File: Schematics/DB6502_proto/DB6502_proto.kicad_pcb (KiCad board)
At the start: 2 copper layers, 132.1 x 104.1 mm, 51 parts, among them J1 System Bus, J10 AVR-ISP-6, J2 Controls, J3 Debug UART, J4 I/O Bus, J5 USB_B, SW1 Reset, U1 DS1813, U2 65C02S, U3 62256, U4 ATmega644PA-PU, U5 62256, U6 74AC138, U7 28C256, U8 22V10C, U9 FT230XS, Y1 20MHz

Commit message: PCB layout RC1
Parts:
- added REF**: OSHW-Logo_5.7x6mm_SilkScreen, Symbol:OSHW-Logo_5.7x6mm_SilkScreen, F.Cu at (71.1, 24.1)
- added REF**: KiCad-Logo2_5mm_SilkScreen, Symbol:KiCad-Logo2_5mm_SilkScreen, F.Cu at (48.9, 49.5)
- moved C3 49.4 mm to (76.2, 104.1), turned to 0 degrees
- moved C9 48.4 mm to (119.4, 80.0), turned to 90 degrees
- moved C1 3.73 mm to (106.6, 104.1), turned to 180 degrees
- moved C10 2.50 mm to (81.3, 45.7), turned to 270 degrees
- moved C5 2.50 mm to (119.4, 54.6), turned to 270 degrees
- moved C8 2.50 mm to (119.4, 31.8), turned to 270 degrees
- moved C2 1.31 mm to (83.8, 104.1)
- moved REF** 0.63 mm to (43.2, 17.8)
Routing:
- net +5V: track 0.00 -> 473.8 mm, vias 0 -> 12
- net d1: track 0.00 -> 288.2 mm, vias 0 -> 6
- net d0: track 0.00 -> 279.0 mm, vias 0 -> 6
- net ~6502_RES: track 0.00 -> 265.6 mm, vias 0 -> 8
- net d5: track 0.00 -> 261.4 mm, vias 0 -> 1
- net d2: track 0.00 -> 261.3 mm, vias 0 -> 4
- net d3: track 0.00 -> 252.5 mm, vias 0 -> 2
- net d6: track 0.00 -> 248.9 mm, vias 0 -> 2
- net d4: track 0.00 -> 246.8 mm, vias 0 -> 2
- net GND: track 0.00 -> 240.7 mm, vias 0 -> 5
- net d7: track 0.00 -> 239.2 mm, vias 0 -> 3
- net R~W: track 0.00 -> 237.7 mm, vias 0 -> 9
- net a0: track 0.00 -> 230.9 mm, vias 0 -> 6
- net a1: track 0.00 -> 228.6 mm, vias 0 -> 6
- net a2: track 0.00 -> 221.5 mm, vias 0 -> 6
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- added copper zone on B.Cu, net GND
- added copper zone on F.Cu, net GND
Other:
- board size 132.1 x 104.1 mm -> 133.3 x 105.4 mm
- net class Default: clearance 0.2 -> 0.1; trace_width 0.25 -> 0.2; via_dia 0.8 -> 0.6
- net class POWER added: clearance 0.1, trace_width 0.25, via_dia 0.6, via_drill 0.4
- rule trace_clearance: 0.2 -> 0.1
- board text added: "+5V"
- board text added: "20MHz"
- board text added: "32KB RAM1"
- board text added: "32KB RAM2"
- board text added: "32KB ROM"
- board text added: "6502 CPU"
- board text added: "6502 Prototype Board Designed by Dawid Buchwald https://github.com/dbuchwald/6502"
- board text added: "A00"
- board text added: "A01"
- board text added: "A02"
- board text added: "A03"
- board text added: "A04"
- board text added: "A05"
- board text added: "A06"
- board text added: "A07"
- board text added: "A08"
- board text added: "A09"
- board text added: "A10"
- board text added: "A11"
- board text added: "A12"
- board text added: "A13"
- board text added: "A14"
- board text added: "A15"
- board text added: "ATmega644PA Supervisor"
- board text added: "AVR ISP"
- board text added: "BE"
- board text added: "CLD"
- board text added: "CLK"
- board text added: "Control Bus"
- board text added: "Control pull-up resistors"
- board text added: "D0"
- board text added: "D1"
- board text added: "D2"
- board text added: "D3"
- board text added: "D4"
- board text added: "D5"
- board text added: "D6"
- board text added: "D7"
- board text added: "EXR"
- board text added: "GND"
- board text added: "I/O Selector"
- board text added: "I12"
- board text added: "IO"
- board text added: "Input/Output Bus"
- board text added: "O13"
- board text added: "O14"
- board text added: "O15"
- board text added: "O16"
- board text added: "Programmable Logic Array"
- board text added: "RDY"
- board text added: "RESET"
- board text added: "RxD"
- board text added: "R~W"
- board text added: "SNC"
- board text added: "SRC"
- board text added: "SRD"
- board text added: "SRO"
- board text added: "System Bus"
- board text added: "TxD"
- board text added: "UART"
- board text added: "USB"
- board text added: "~6RS"
- board text added: "~CTS"
- board text added: "~IO0"
- board text added: "~IO1"
- board text added: "~IO2"
- board text added: "~IO3"
- board text added: "~IRQ"
- board text added: "~LAT"
- board text added: "~ML"
- board text added: "~NMI"
- board text added: "~OE"
- board text added: "~RES"
- board text added: "~RM1"
- board text added: "~RM2"
- board text added: "~ROM"
- board text added: "~RST"
- board text added: "~RTS"
- board text added: "~SO"
- board text added: "~URT"
- board text added: "~VI1"
- board text added: "~VI2"
- board text added: "~VP"
- board text added: "~WE"

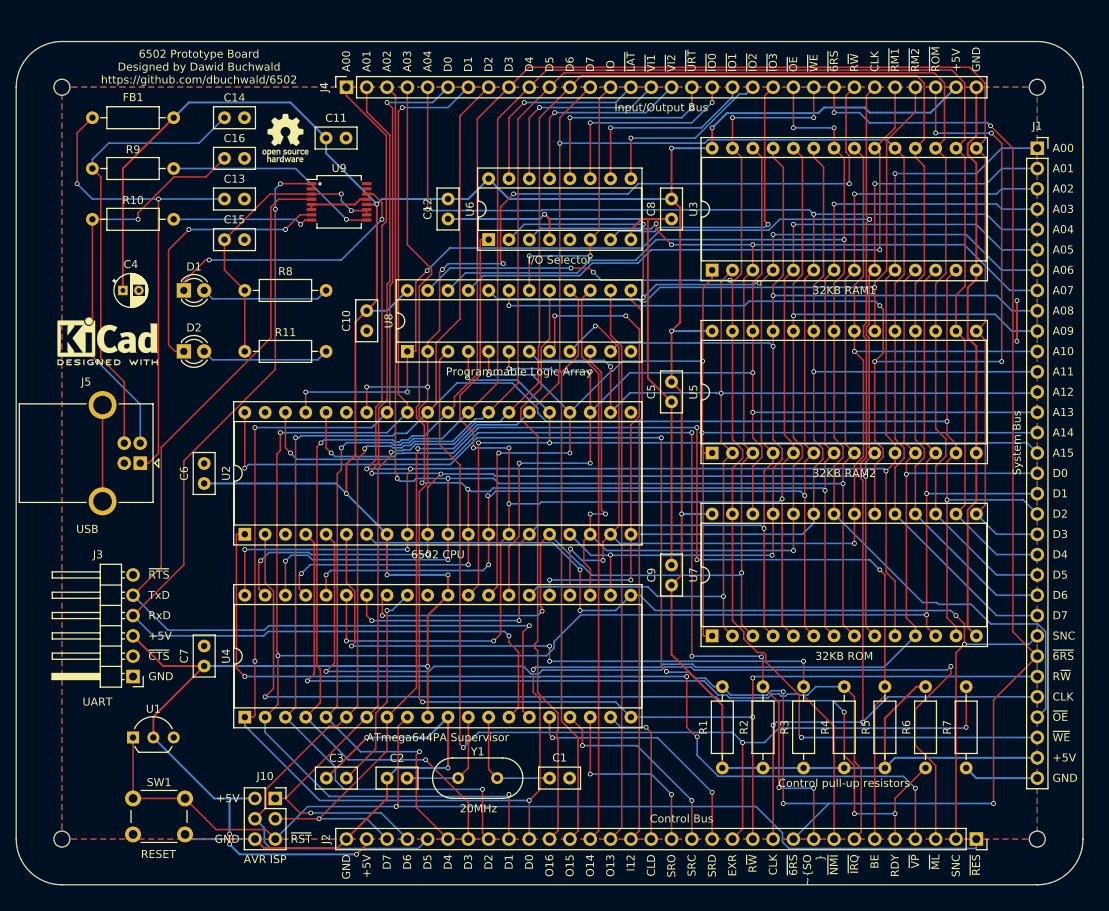
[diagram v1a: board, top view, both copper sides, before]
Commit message: Ordered DB6502 proto PCB
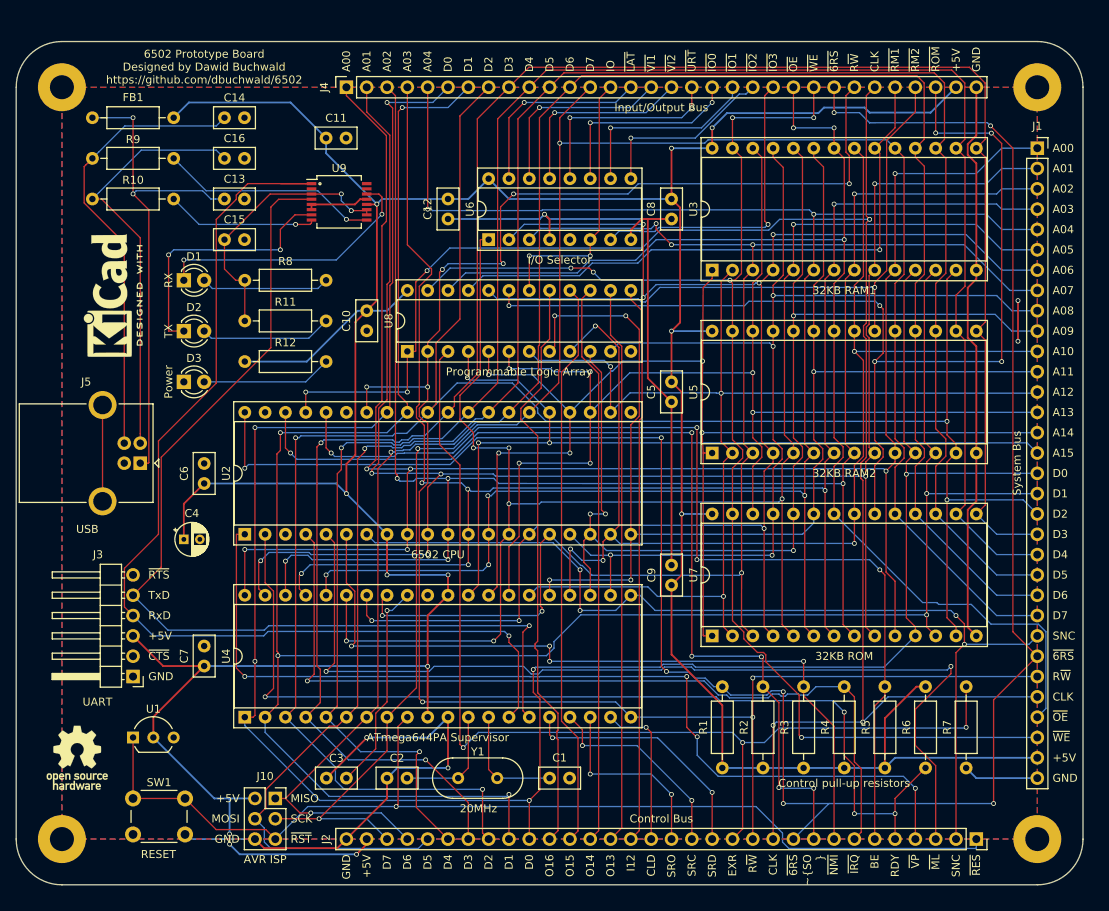
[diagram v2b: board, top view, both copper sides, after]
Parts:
- removed the REF** at (71.1, 24.1)
- removed the REF** at (48.9, 49.5)
- removed the REF** at (43.2, 17.8)
- removed the REF** at (43.2, 111.8)
- removed the REF** at (165.1, 111.8)
- removed the REF** at (165.1, 17.8)
- added D3: PWR, LED_THT:LED_D3.0mm, F.Cu at (58.4, 54.6)
- added R12: 220, Resistor_THT:R_Axial_DIN0207_L6.3mm_D2.5mm_P10.16mm_Horizontal, F.Cu at (66.0, 52.1)
- added REF**: OSHW-Logo_7.5x8mm_SilkScreen, Symbol:OSHW-Logo_7.5x8mm_SilkScreen, F.Cu at (45.1, 101.6)
- added REF**: KiCad-Logo2_6mm_SilkScreen, Symbol:KiCad-Logo2_6mm_SilkScreen, F.Cu at (48.9, 43.8)
- added REF**: MountingHole_3mm_Pad, MountingHole:MountingHole_3mm_Pad, F.Cu at (43.2, 111.8)
- added REF**: MountingHole_3mm_Pad, MountingHole:MountingHole_3mm_Pad, F.Cu at (165.1, 111.8)
- added REF**: MountingHole_3mm_Pad, MountingHole:MountingHole_3mm_Pad, F.Cu at (165.1, 17.8)
- added REF**: MountingHole_3mm_Pad, MountingHole:MountingHole_3mm_Pad, F.Cu at (43.2, 17.8)
- moved C4 32.0 mm to (58.4, 74.3)
- moved R11 3.81 mm to (66.0, 47.0)
- moved D2 2.54 mm to (58.4, 48.3)
- moved R10 2.54 mm to (47.0, 31.8)
- moved D1 1.27 mm to (58.4, 41.9)
- moved R8 1.27 mm to (66.0, 41.9)
- moved R9 1.27 mm to (47.0, 26.7)
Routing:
- net Net-(D3-Pad2): track 0.00 -> 16.3 mm
- net RxD_DBG: track 125.1 -> 132.3 mm, vias 3 -> 1
- net Net-(C15-Pad1): track 37.2 -> 34.1 mm
- net Net-(C16-Pad1): track 50.6 -> 53.1 mm, vias 2 -> 0
- net +5V: track 473.8 -> 475.5 mm
- net USBD+: track 17.8 -> 19.0 mm
- net ~TXLED: track 33.8 -> 32.9 mm
- net Net-(C14-Pad1): track 55.8 -> 56.7 mm
- net Net-(C13-Pad1): track 62.8 -> 62.1 mm
- net USBD-: track 26.8 -> 27.3 mm
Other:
- net class Default: clearance 0.1 -> 0.1524; trace_width 0.2 -> 0.1524
- net class POWER: clearance 0.1 -> 0.1524; trace_width 0.25 -> 0.2286
- rule trace_clearance: 0.1 -> 0.1524
- rule trace_min: 0.2 -> 0.1524
- board text added: "MISO"
- board text added: "MOSI"
- board text added: "Power"
- board text added: "RX"
- board text added: "SCK"
- board text added: "TX"
